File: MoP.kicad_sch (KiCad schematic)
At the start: 0 parts

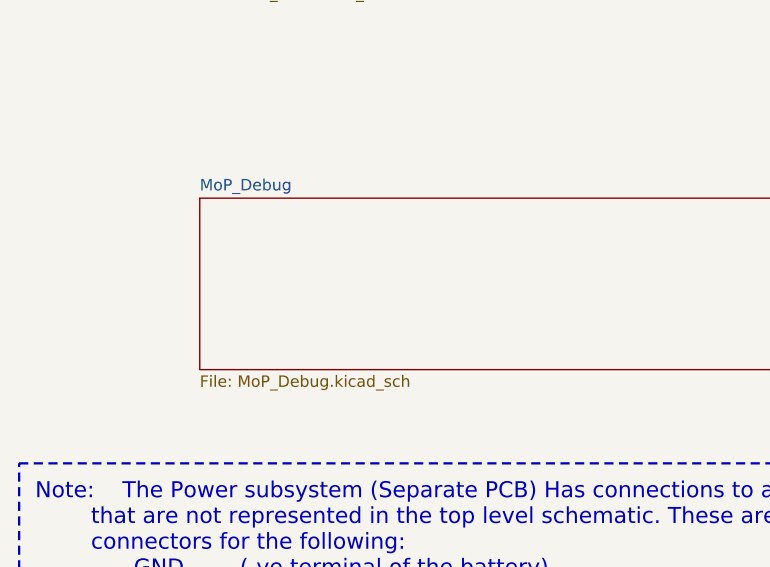
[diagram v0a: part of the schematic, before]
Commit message: added SPI and I2C hierarchical connectors to sensors sheet and reordered page numbers
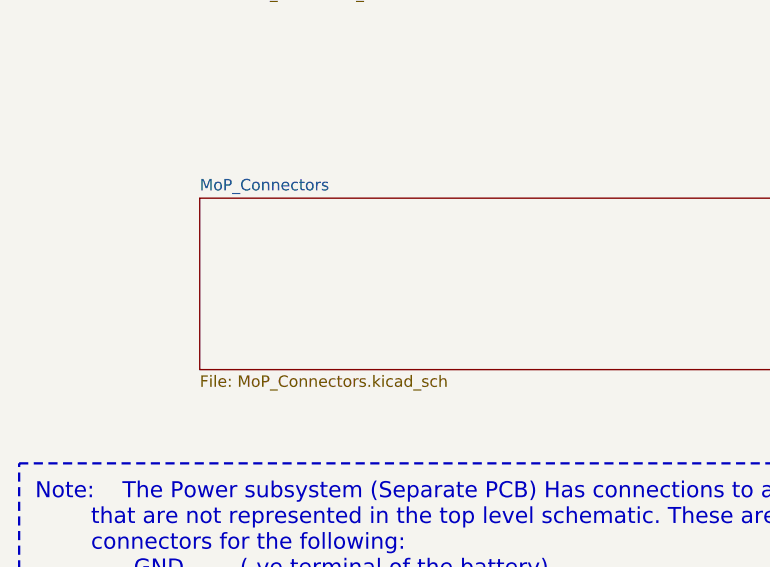
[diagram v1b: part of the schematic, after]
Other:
- sheet MoP_Debug renamed MoP_Connectors
- sheet MoP_Connectors: file MoP_Debug.kicad_sch -> MoP_Connectors.kicad_sch
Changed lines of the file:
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@@
 			(project "MoP"
 				(path "/4d76798e-9a11-4d8d-a723-72f274a89091"
-					(page "9")
+					(page "7")
 				)
 			)
@@
 			(project "MoP"
 				(path "/4d76798e-9a11-4d8d-a723-72f274a89091"
-					(page "10")
+					(page "5")
 				)
 			)
@@
 			(project "MoP"
 				(path "/4d76798e-9a11-4d8d-a723-72f274a89091"
-					(page "8")
+					(page "6")
 				)
 			)
@@
 			(color 0 0 0 0.0000)
 		)
-		(property "Sheetname" "MoP_Debug"
+		(property "Sheetname" "MoP_Connectors"
 			(at 39.37 133.9084 0)
 			(effects
@@
 			)
 		)
-		(property "Sheetfile" "MoP_Debug.kicad_sch"
+		(property "Sheetfile" "MoP_Connectors.kicad_sch"
 			(at 39.37 154.2546 0)
 			(effects
@@
 			(project "MoP"
 				(path "/4d76798e-9a11-4d8d-a723-72f274a89091"
-					(page "13")
+					(page "11")
 				)
 			)
@@
 			(project "MoP"
 				(path "/4d76798e-9a11-4d8d-a723-72f274a89091"
-					(page "10")
+					(page "8")
 				)
 			)
@@
 			(project "MoP"
 				(path "/4d76798e-9a11-4d8d-a723-72f274a89091"
-					(page "7")
+					(page "12")
 				)
 			)
@@
 			(project "MoP"
 				(path "/4d76798e-9a11-4d8d-a723-72f274a89091"
-					(page "11")
+					(page "9")
 				)
 			)
@@
 			(project "MoP"
 				(path "/4d76798e-9a11-4d8d-a723-72f274a89091"
-					(page "5")
+					(page "4")
 				)
 			)
@@
 			(project "MoP"
 				(path "/4d76798e-9a11-4d8d-a723-72f274a89091"
-					(page "15")
-				)
-			)
+					(page "10")
+				)
+			)

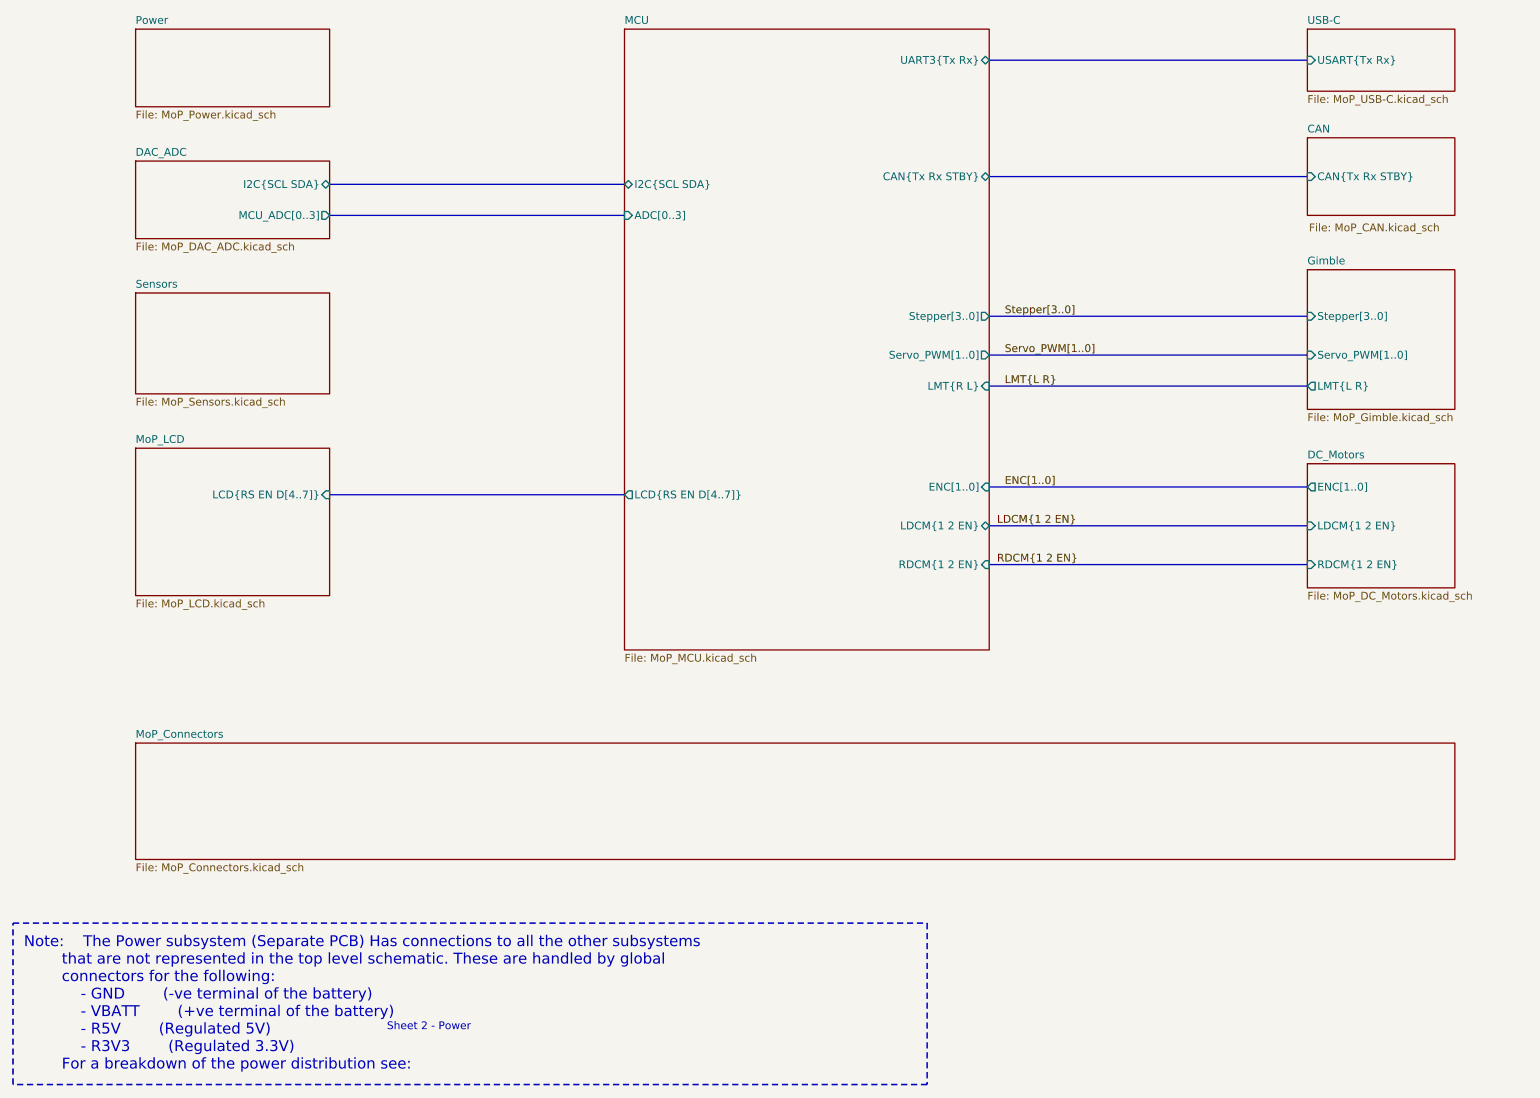
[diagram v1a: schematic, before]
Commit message: changed ref designators to be consistent accross sheets
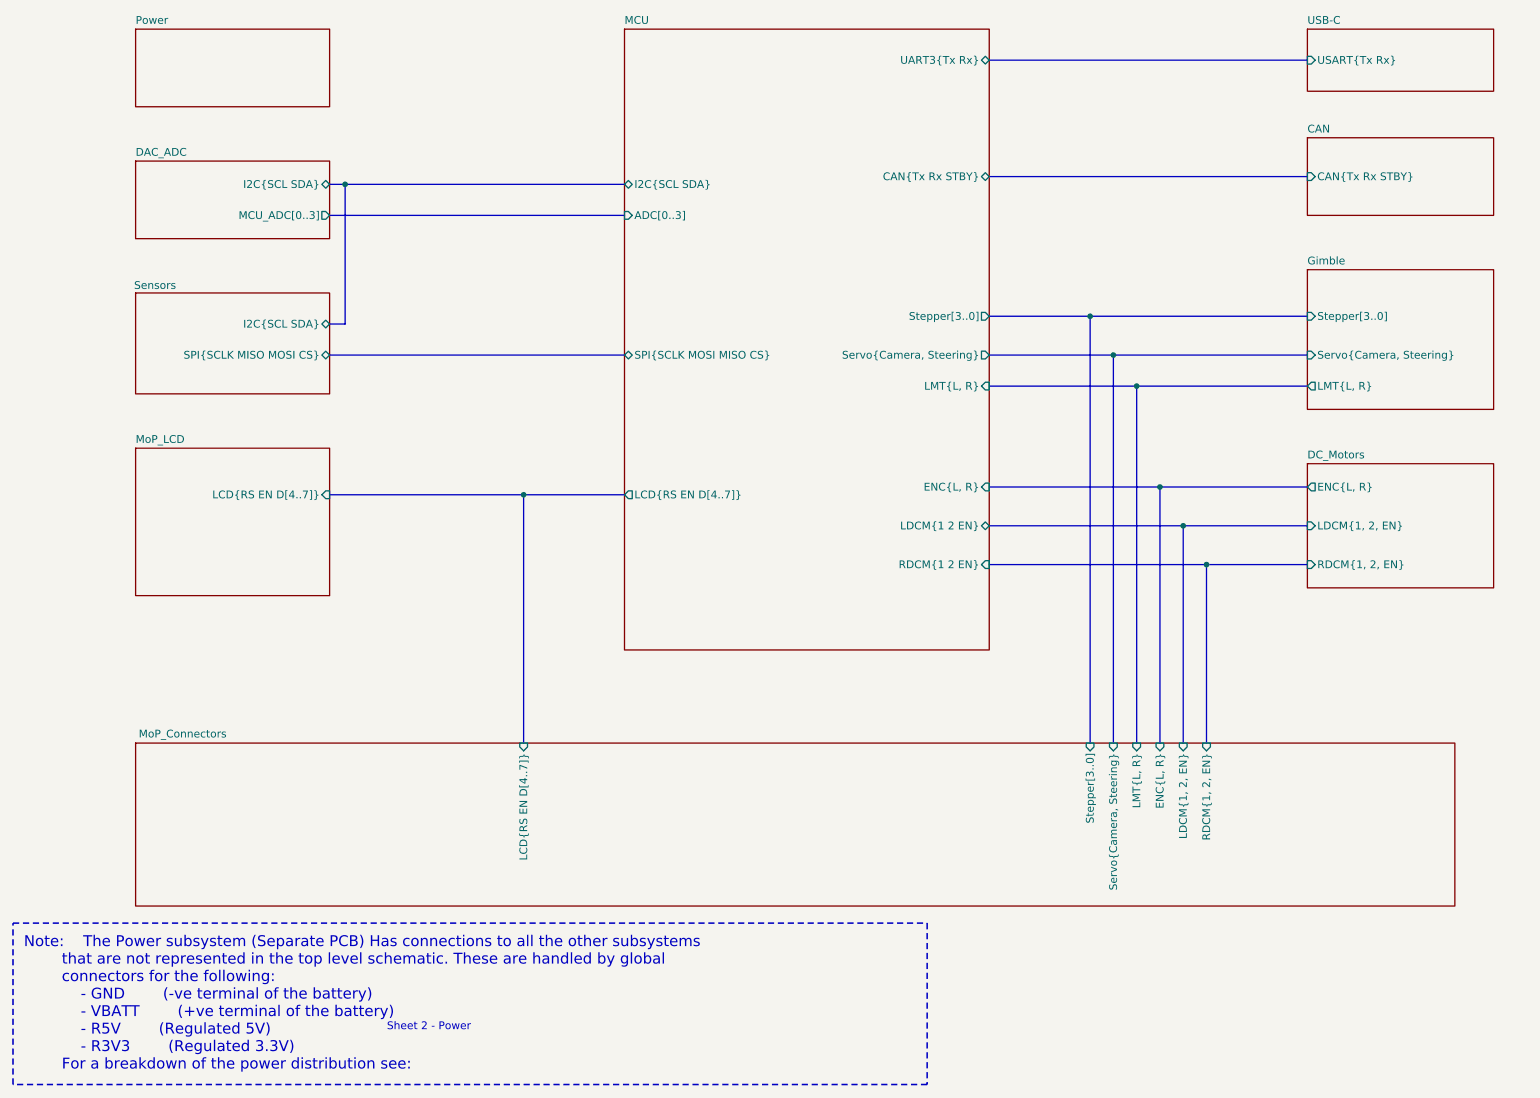
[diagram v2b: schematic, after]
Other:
- sheet DC_Motors ports: added ENC{L, R}, LDCM{1, 2, EN}, RDCM{1, 2, EN}; removed ENC[1..0], LDCM{1 2 EN}, RDCM{1 2 EN}
- sheet Gimble ports: added LMT{L, R}, Servo{Camera, Steering}; removed LMT{L R}, Servo_PWM[1..0]
- sheet MCU ports: added ENC{L, R}, LMT{L, R}, SPI{SCLK MOSI MISO CS}, Servo{Camera, Steering}; removed ENC[1..0], LMT{R L}, Servo_PWM[1..0]
- sheet MoP_Connectors ports: added ENC{L, R}, LCD{RS EN D[4..7]}, LDCM{1, 2, EN}, LMT{L, R}, RDCM{1, 2, EN}, Servo{Camera, Steering}, Stepper[3..0]; removed none
- sheet Sensors ports: added I2C{SCL SDA}, SPI{SCLK MISO MOSI CS}; removed none

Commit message: Finished schematics
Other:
- sheet DAC_ADC ports: added ICHG, PSYS; removed none
- sheet MCU ports: added GPIO[0..16]; removed none
- sheet Power ports: added Alert, I2C{SCL SDA}, ICHG, PSYS, ~{PROCHOT}; removed none

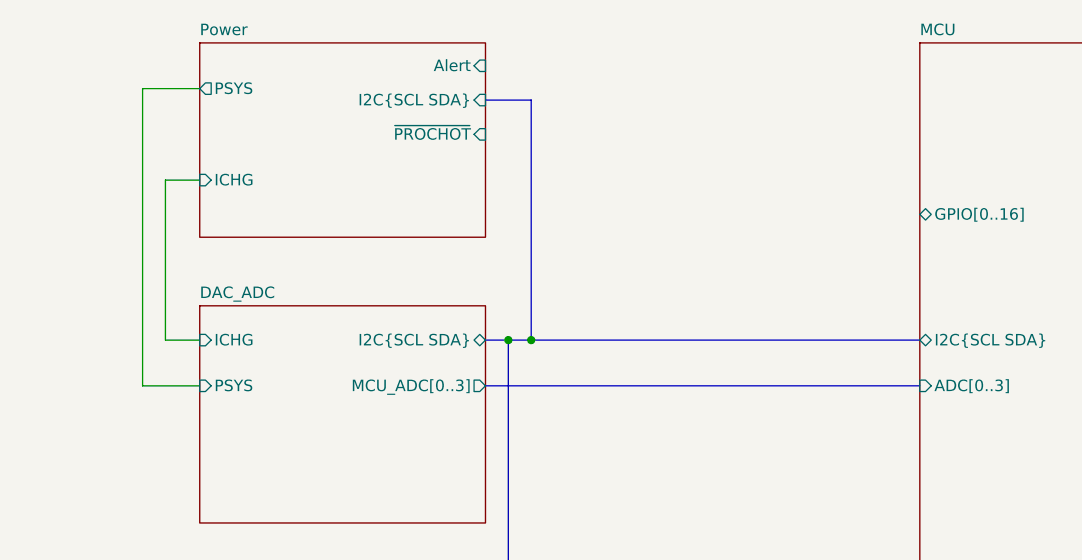
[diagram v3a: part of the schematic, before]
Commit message: Added subproject for EPS PCB
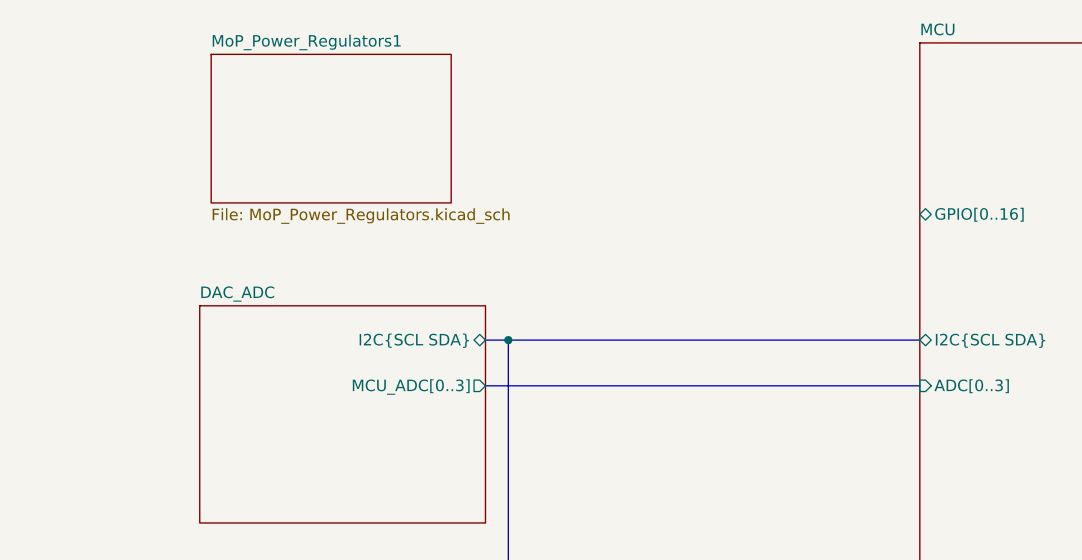
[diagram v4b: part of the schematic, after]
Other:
- removed sheet Power
- added sheet MoP_Power_Regulators1 (MoP_Power_Regulators.kicad_sch)
- sheet DAC_ADC ports: added none; removed ICHG, PSYS
